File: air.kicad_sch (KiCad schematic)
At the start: 31 parts, among them J1 Conn_01x05, J2 Conn_01x05, J3 Conn_01x04, U1 短接, U2 AIR32F103CBT6-LQFP48, U3 RT9013-33GB, U4 USBLC6-2SC6, Y1 8M/20pF

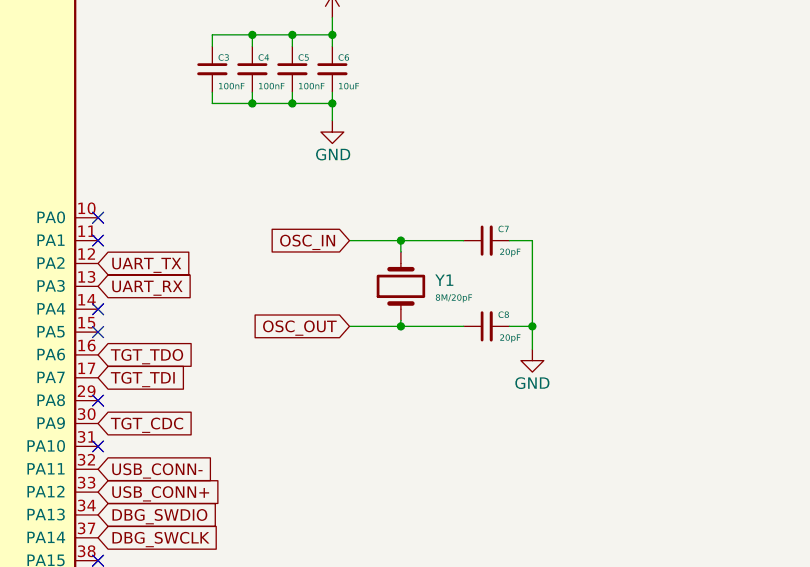
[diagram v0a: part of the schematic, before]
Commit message: V1.3 3225晶振版本
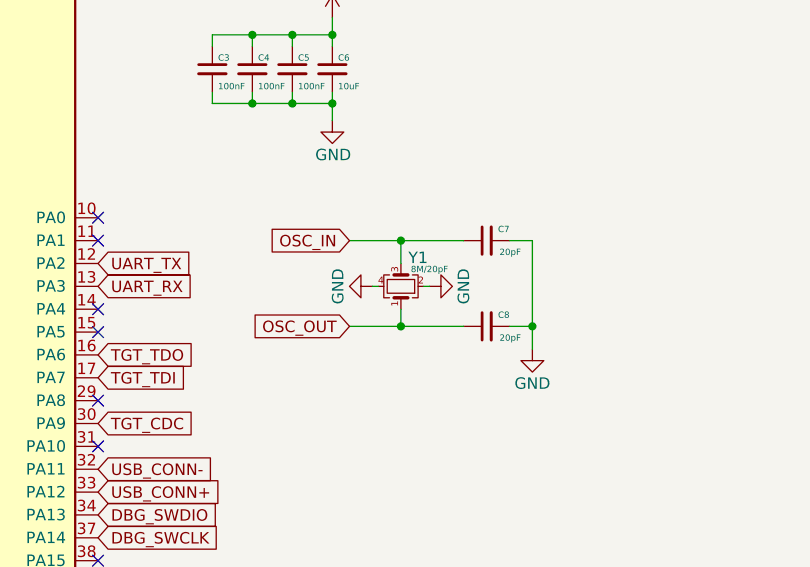
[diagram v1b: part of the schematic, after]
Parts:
- removed Y1: 8M/20pF, Crystal:Crystal_SMD_5032-2Pin_5.0x3.2mm, symbol Device:Crystal
- added Y1: 8M/20pF, Crystal:Crystal_SMD_3225-4Pin_3.2x2.5mm, symbol Device:Crystal_GND24_Small
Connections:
- net GND: now also Y1.2, Y1.4
- net OSC_IN: now also Y1.3
- net OSC_OUT: now also Y1.1
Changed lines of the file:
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@@
+    (stroke (width 0) (type default) (color 0 0 0 0))
+  )
+  (wire (pts (xy 123.19 79.375) (xy 123.825 79.375))
     (stroke (width 0) (type default) (color 0 0 0 0))
   )
@@
     (stroke (width 0) (type default) (color 0 0 0 0))
   )
-  (wire (pts (xy 120.65 83.185) (xy 120.65 83.82))
+  (wire (pts (xy 120.65 81.915) (xy 120.65 83.82))
     (stroke (width 0) (type default) (color 0 0 0 0))
   )
@@
     (stroke (width 0) (type default) (color 0 0 0 0))
   )
-  (wire (pts (xy 120.65 74.295) (xy 120.65 75.565))
+  (wire (pts (xy 120.65 74.295) (xy 120.65 76.835))
     (stroke (width 0) (type default) (color 0 0 0 0))
   )
@@
   )
   (wire (pts (xy 222.885 66.675) (xy 227.33 66.675))
+    (stroke (width 0) (type default) (color 0 0 0 0))
+  )
+  (wire (pts (xy 117.475 79.375) (xy 118.11 79.375))
     (stroke (width 0) (type default) (color 0 0 0 0))
   )
@@
     )
   )
+  (symbol (lib_id "Device:Crystal_GND24_Small") (at 120.65 79.375 90) (unit 1)
+    (in_bom yes) (on_board yes)
+    (property "Reference" "Y1" (id 0) (at 122.555 76.2 90))
+    (property "Value" "8M/20pF" (id 1) (at 123.825 77.47 90)
+      (effects (font (size 0.7 0.7)))
+    )
+    (property "Footprint" "Crystal:Crystal_SMD_3225-4Pin_3.2x2.5mm" (id 2) (at 120.65 79.375 0)
+      (effects (font (size 1.27 1.27)) hide)
+    )
+    (property "Datasheet" "~" (id 3) (at 120.65 79.375 0)
+      (effects (font (size 1.27 1.27)) hide)
+    )
+    (pin "1")
+    (pin "2")
+    (pin "3")
+    (pin "4")
+  )
   (symbol (lib_id "power:GND") (at 172.085 133.985 270) (unit 1)
     (in_bom yes) (on_board yes)
@@
     )
     (property "Datasheet" "~" (id 3) (at 252.73 88.265 0)
-      (effects (font (size 1.27 1.27)) hide)
-    )
-    (pin "1")
-    (pin "2")
-  )
-  (symbol (lib_id "Device:Crystal") (at 120.65 79.375 90) (unit 1)
-    (in_bom yes) (on_board yes) (fields_autoplaced)
-    (property "Reference" "Y1" (id 0) (at 124.46 78.7399 90)
-      (effects (font (size 1.27 1.27)) (justify right))
-    )
-    (property "Value" "8M/20pF" (id 1) (at 124.46 80.645 90)
-      (effects (font (size 0.7 0.7)) (justify right))
-    )
-    (property "Footprint" "Crystal:Crystal_SMD_5032-2Pin_5.0x3.2mm" (id 2) (at 120.65 79.375 0)
-      (effects (font (size 1.27 1.27)) hide)
-    )
-    (property "Datasheet" "~" (id 3) (at 120.65 79.375 0)
       (effects (font (size 1.27 1.27)) hide)
     )
@@
     (pin "2")
   )
+  (symbol (lib_id "power:GND") (at 117.475 79.375 270) (unit 1)
+    (in_bom yes) (on_board yes)
+    (property "Reference" "#PWR0103" (id 0) (at 111.125 79.375 0)
+      (effects (font (size 1.27 1.27)) hide)
+    )
+    (property "Value" "GND" (id 1) (at 113.665 79.375 0))
+    (property "Footprint" "" (id 2) (at 117.475 79.375 0)
+      (effects (font (size 1.27 1.27)) hide)
+    )
+    (property "Datasheet" "" (id 3) (at 117.475 79.375 0)
+      (effects (font (size 1.27 1.27)) hide)
+    )
+    (pin "1")
+  )
   (symbol (lib_id "Connector_Generic:Conn_01x05") (at 240.665 121.285 0) (unit 1)
     (in_bom yes) (on_board yes) (fields_autoplaced)
@@
     (pin "2")
   )
+  (symbol (lib_id "power:GND") (at 123.825 79.375 90) (unit 1)
+    (in_bom yes) (on_board yes)
+    (property "Reference" "#PWR0102" (id 0) (at 130.175 79.375 0)
+      (effects (font (size 1.27 1.27)) hide)
+    )
+    (property "Value" "GND" (id 1) (at 127.635 79.375 0))
+    (property "Footprint" "" (id 2) (at 123.825 79.375 0)
+      (effects (font (size 1.27 1.27)) hide)
+    )
+    (property "Datasheet" "" (id 3) (at 123.825 79.375 0)
+      (effects (font (size 1.27 1.27)) hide)
+    )
+    (pin "1")
+  )
   (symbol (lib_id "Device:C_Small") (at 104.14 55.245 0) (unit 1)
     (in_bom yes) (on_board yes)
@@
       (reference "#PWR0101") (unit 1) (value "+3.3V") (footprint "")
     )
+    (path "/96305177-eb01-4b40-aa3e-6e3737c14456"
+      (reference "#PWR0102") (unit 1) (value "GND") (footprint "")
+    )
+    (path "/4be62063-2f7e-42bb-8d55-62b5c85fcde6"
+      (reference "#PWR0103") (unit 1) (value "GND") (footprint "")
+    )
     (path "/8ca3543b-551e-4770-8a11-6efc6d0ea476"
       (reference "C1") (unit 1) (value "100nF") (footprint "Capacitor_SMD:C_0603_1608Metric")
@@
       (reference "USB1") (unit 1) (value "TYPE-C_16P(073)") (footprint "Shaojie_Custom:USB-C-SMD_TYPE-C16PIN_C668624")
     )
-    (path "/182d9005-5882-4e6a-b349-b4fd884620e2"
-      (reference "Y1") (unit 1) (value "8M/20pF") (footprint "Crystal:Crystal_SMD_5032-2Pin_5.0x3.2mm")
-    )
-  )
+    (path "/0277a71e-cd15-4b84-899e-8eff273fa6ec"
+      (reference "Y1") (unit 1) (value "8M/20pF") (footprint "Crystal:Crystal_SMD_3225-4Pin_3.2x2.5mm")
+    )
+  )

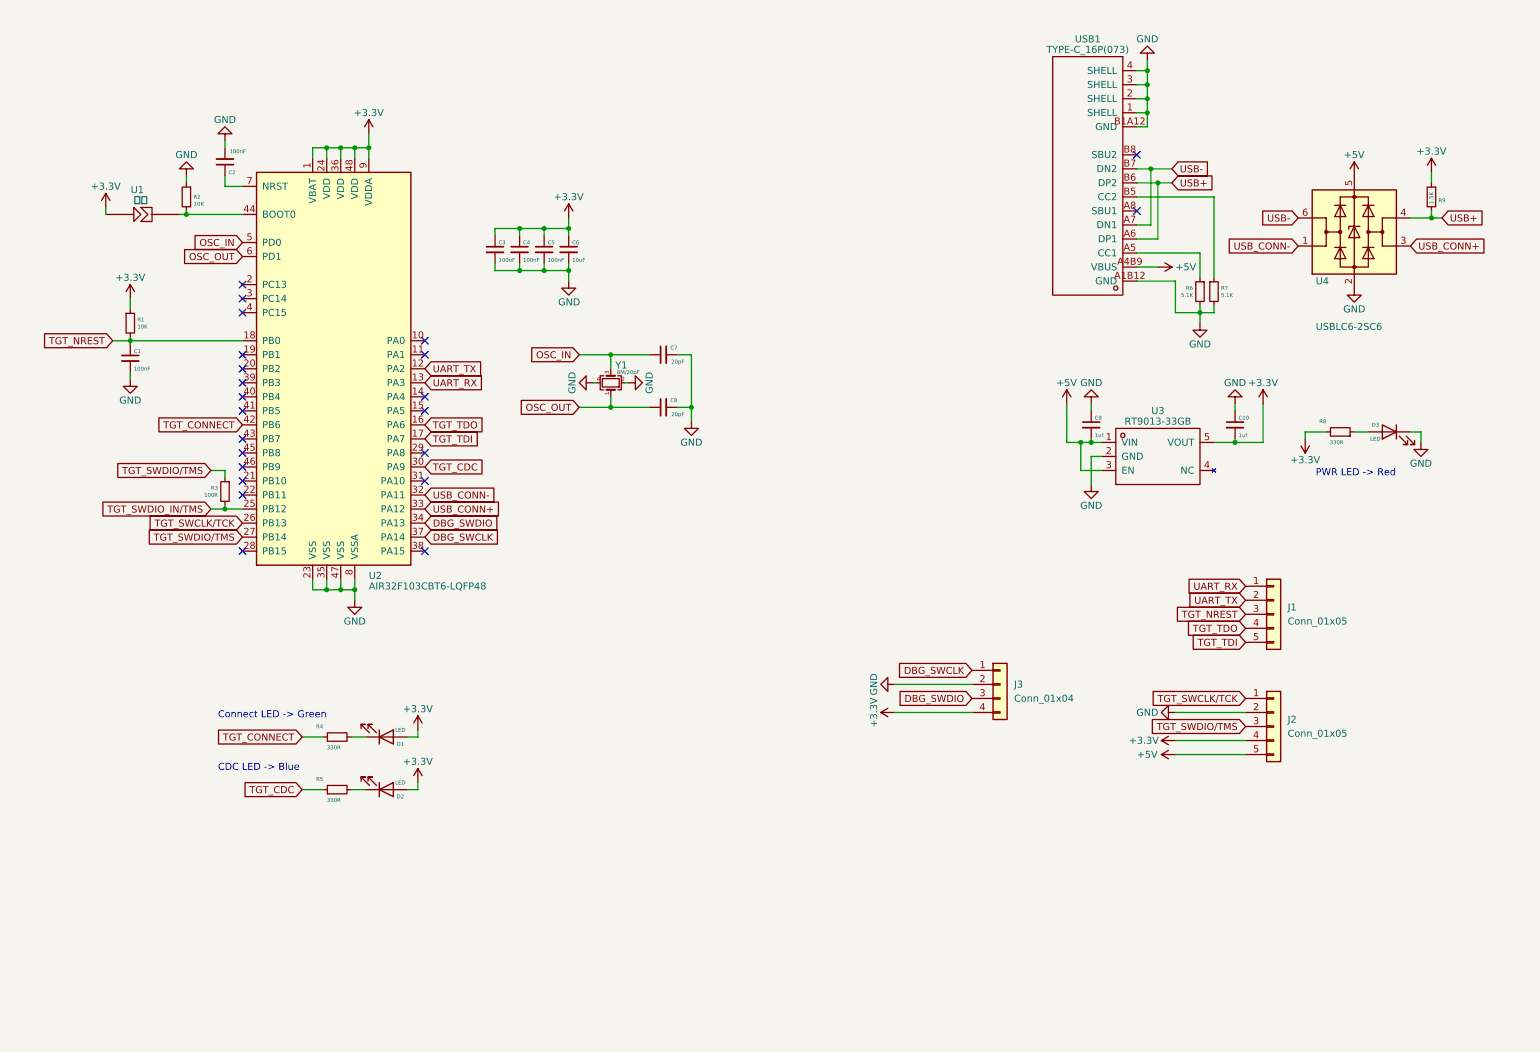
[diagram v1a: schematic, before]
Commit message: 更新了SWO的硬件功能 从该板开始 可能不兼容上一代的固件
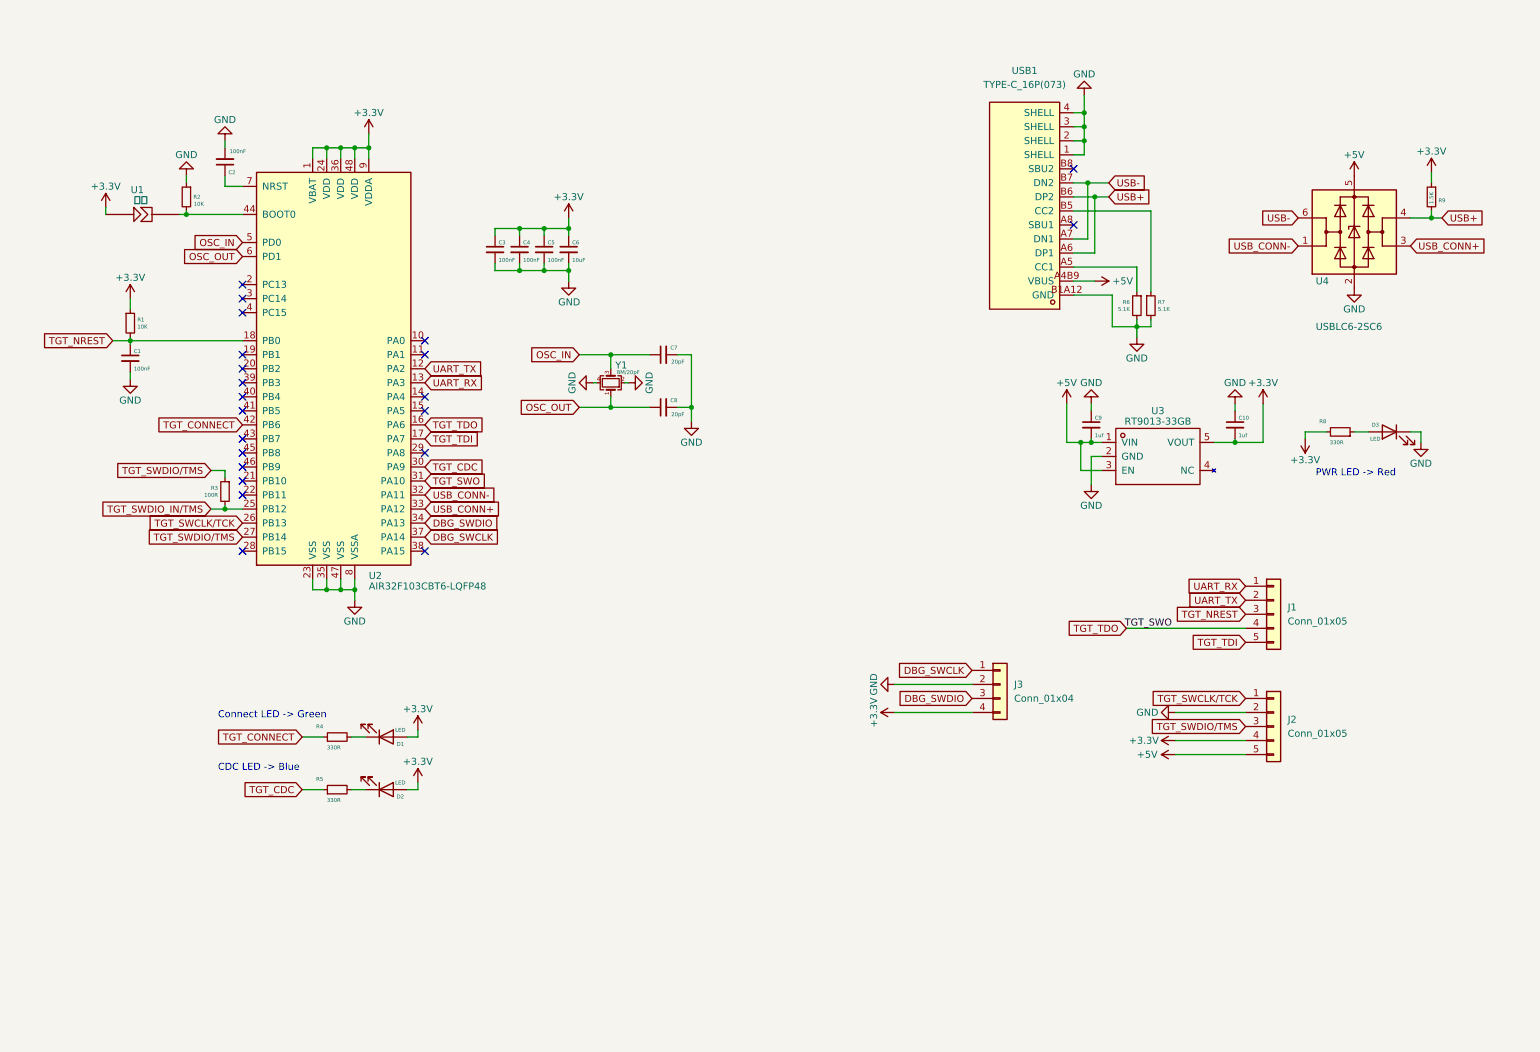
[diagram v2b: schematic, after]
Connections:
- net TGT_TDO is gone; now on net TGT_SWO: J1.4 (Pin_4), U2.16 (PA6)
- net TGT_SWO: now reaches U2.31 (PA10)
- no-connect marks 23 -> 22
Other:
- moved on the sheet: R6, R7
